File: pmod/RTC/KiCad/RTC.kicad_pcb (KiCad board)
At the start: 2 copper layers, 35 x 12 mm, 5 parts, among them J1 Conn_01x04, J2 Conn_01x04, J3 Conn_01x04

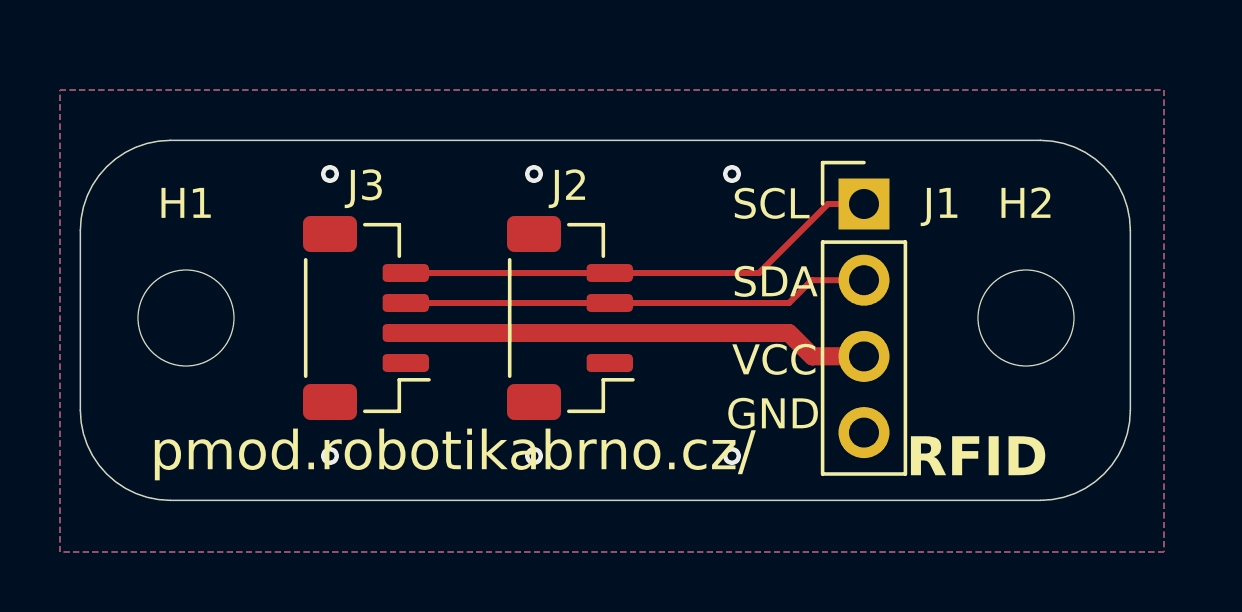
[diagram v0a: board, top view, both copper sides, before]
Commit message: fix: Pridal jsem opravy, ktere byly navrzene
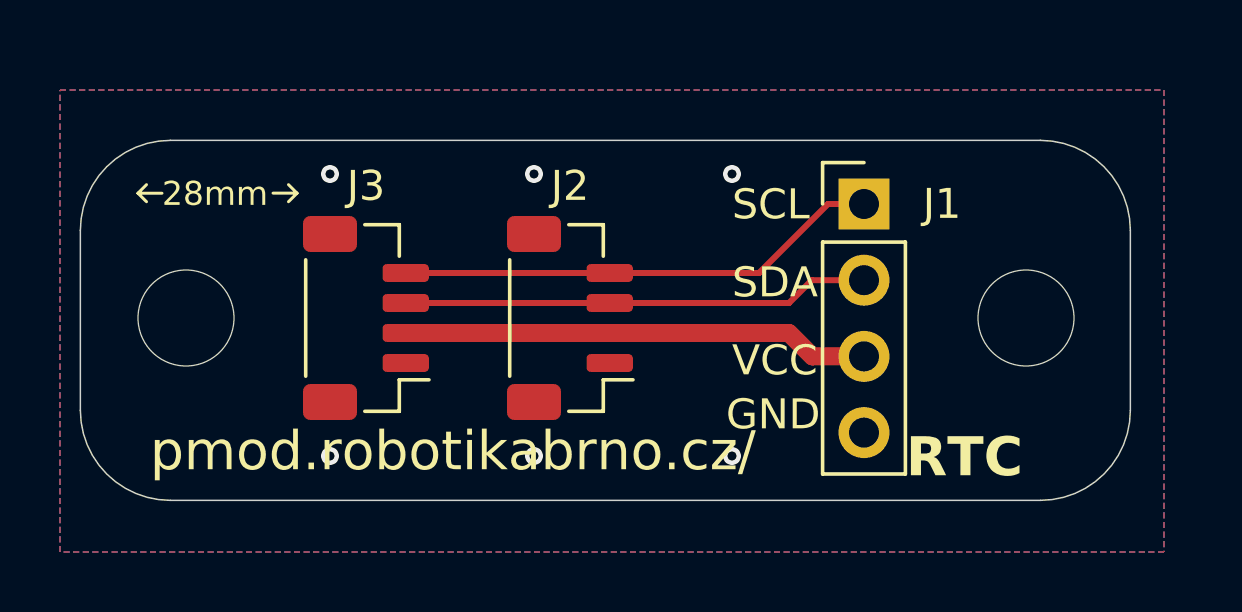
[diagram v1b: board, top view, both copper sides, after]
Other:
- board text added: "28mm"
- board text added: "RTC"
- board text removed: "RFID"

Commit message: fix: prepare all board for manufacturing
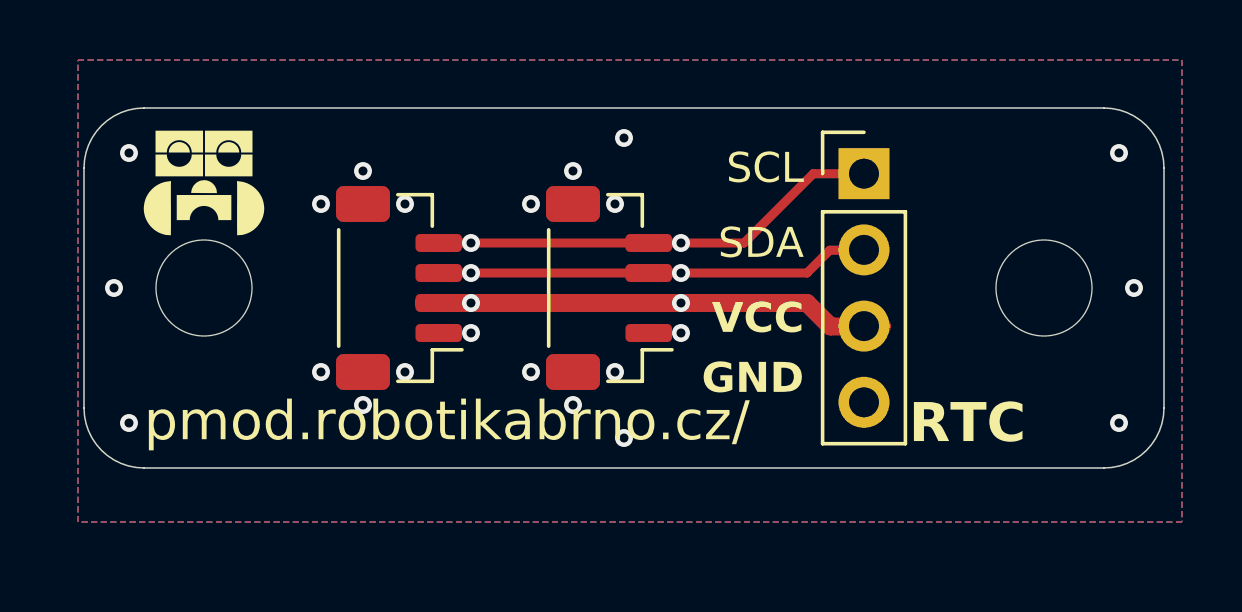
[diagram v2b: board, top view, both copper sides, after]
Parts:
- H1, H2: footprint MountingHole:MountingHole_3.2mm_M3_DIN965 -> MountingHole:MountingHole_3.2mm_M3
- moved J2 1.64 mm to (144.5, 79.0)
- moved J3 1.49 mm to (137.5, 79.0)
- moved H1 1.17 mm to (131.0, 79.0)
- moved H2 1.17 mm to (159.0, 79.0)
- moved J1 1.01 mm to (153.0, 75.2)
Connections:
- J2 pad MP: (no net) -> GND
- J3 pad MP: (no net) -> GND
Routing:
- net Net-(J1-Pin_1): vias 0 -> 2
- net Net-(J1-Pin_2): vias 0 -> 2
- net VCC: vias 0 -> 2
- net GND: vias 6 -> 22
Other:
- board size 35 x 12 mm -> 36 x 12 mm
- board text added: "12mm"
- board text added: "36mm"
- board text removed: "28mm"
